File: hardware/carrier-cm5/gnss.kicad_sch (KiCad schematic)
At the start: 18 parts, among them J40 U.FL GNSS, J41 GNSS module, U40 MAX-M10S-00B

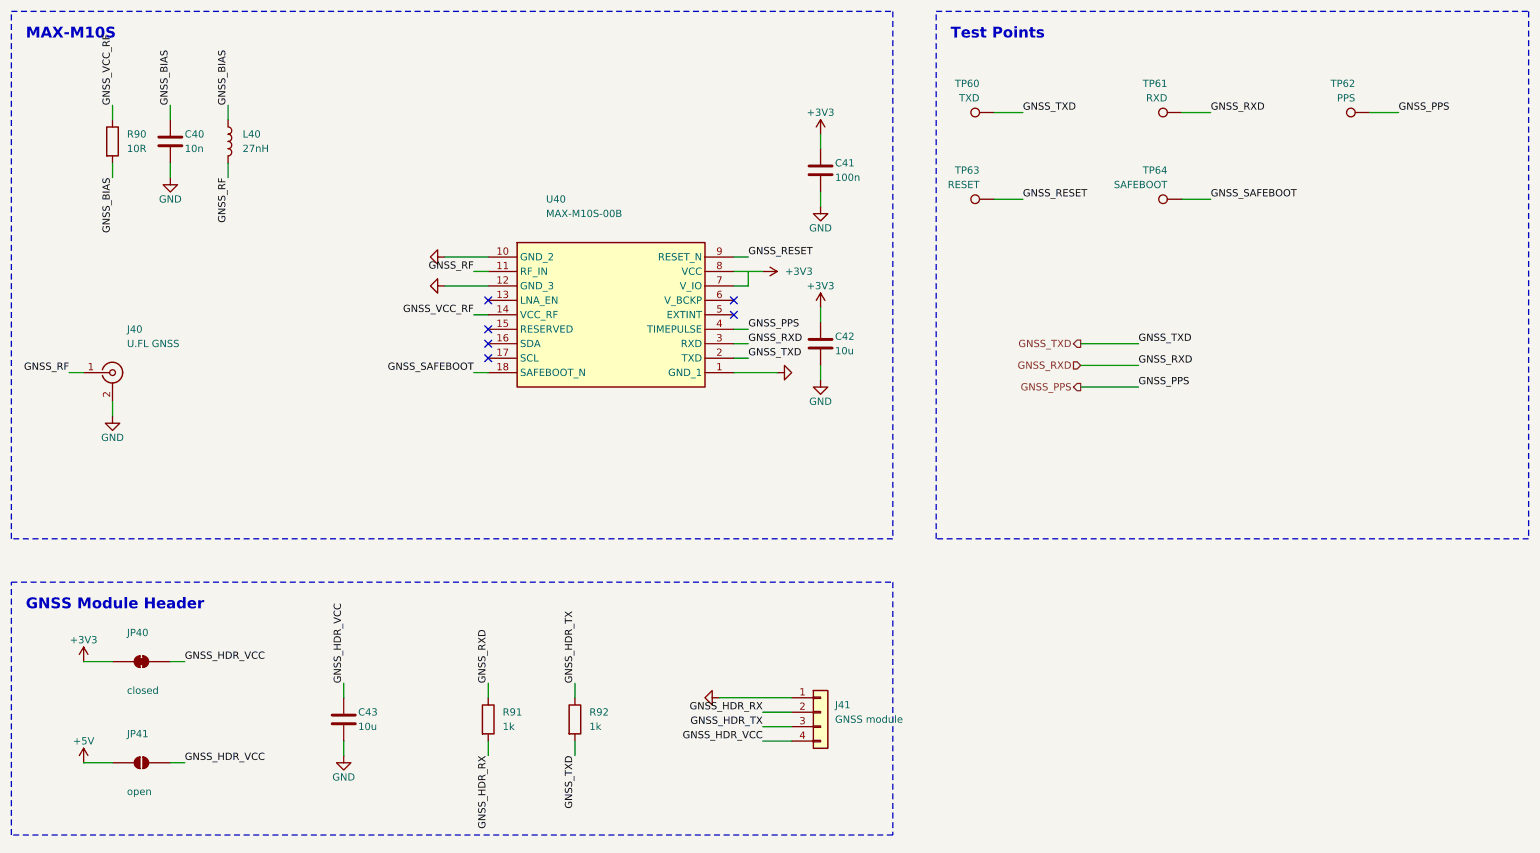
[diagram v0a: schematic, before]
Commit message: Updated schematic on CM5 carrier
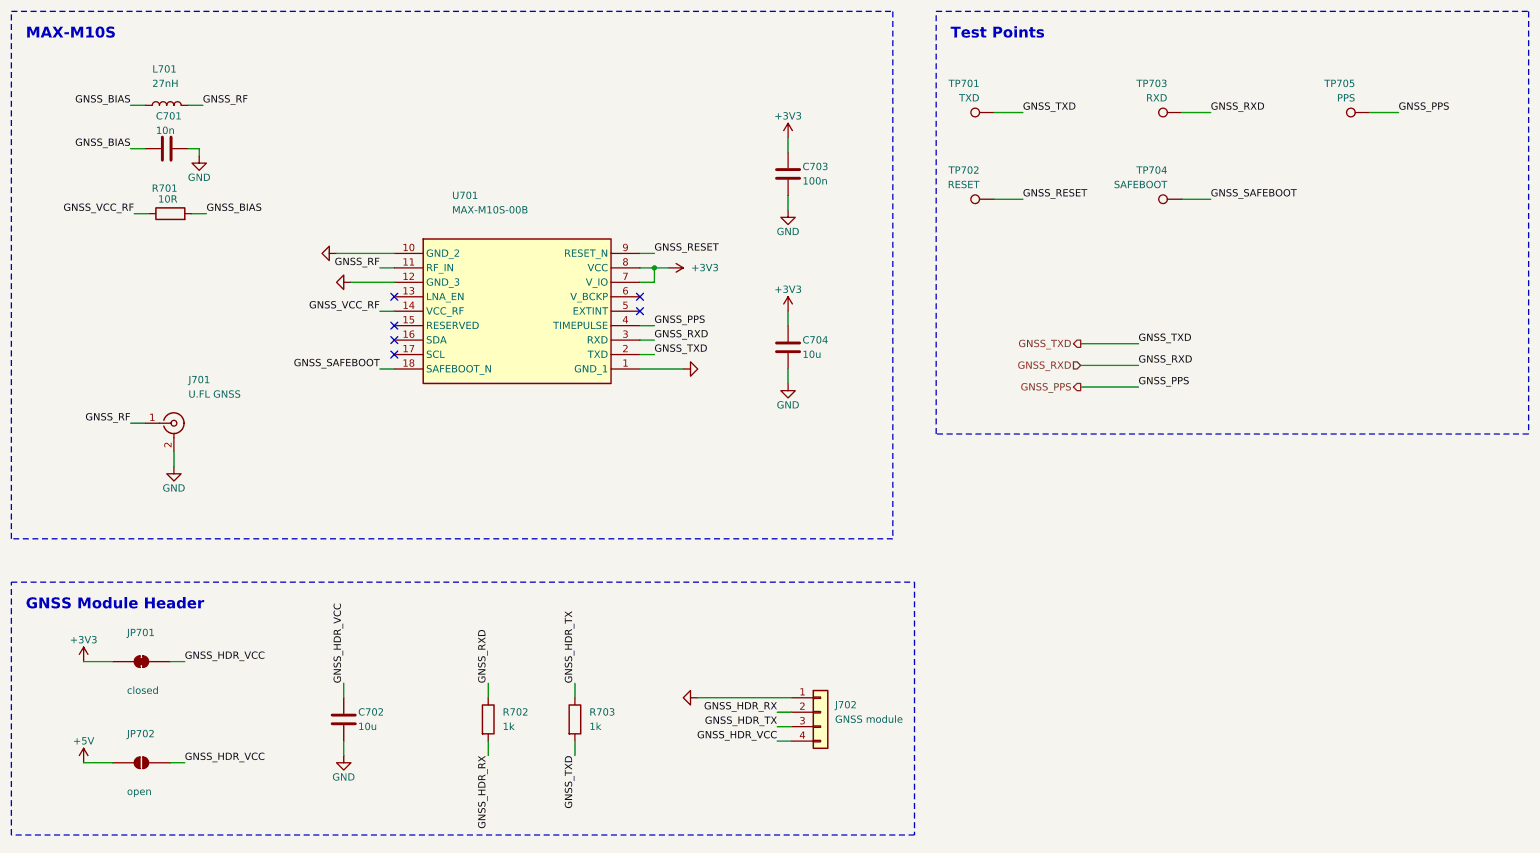
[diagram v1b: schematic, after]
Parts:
- renumbered C40 to C701, C43 to C702, C41 to C703, C42 to C704, J40 to J701, J41 to J702, JP40 to JP701, JP41 to JP702, L40 to L701, R90 to R701, R91 to R702, R92 to R703, TP60 to TP701, TP63 to TP702, TP61 to TP703, TP64 to TP704, TP62 to TP705, U40 to U701
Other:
- company: AAC -> (none)
- moved on the sheet: C701, C703, C704, J701, L701, R701, U701
